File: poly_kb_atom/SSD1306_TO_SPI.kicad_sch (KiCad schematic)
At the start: 11 parts, among them J1 Conn_01x16, SW1 SW_Push

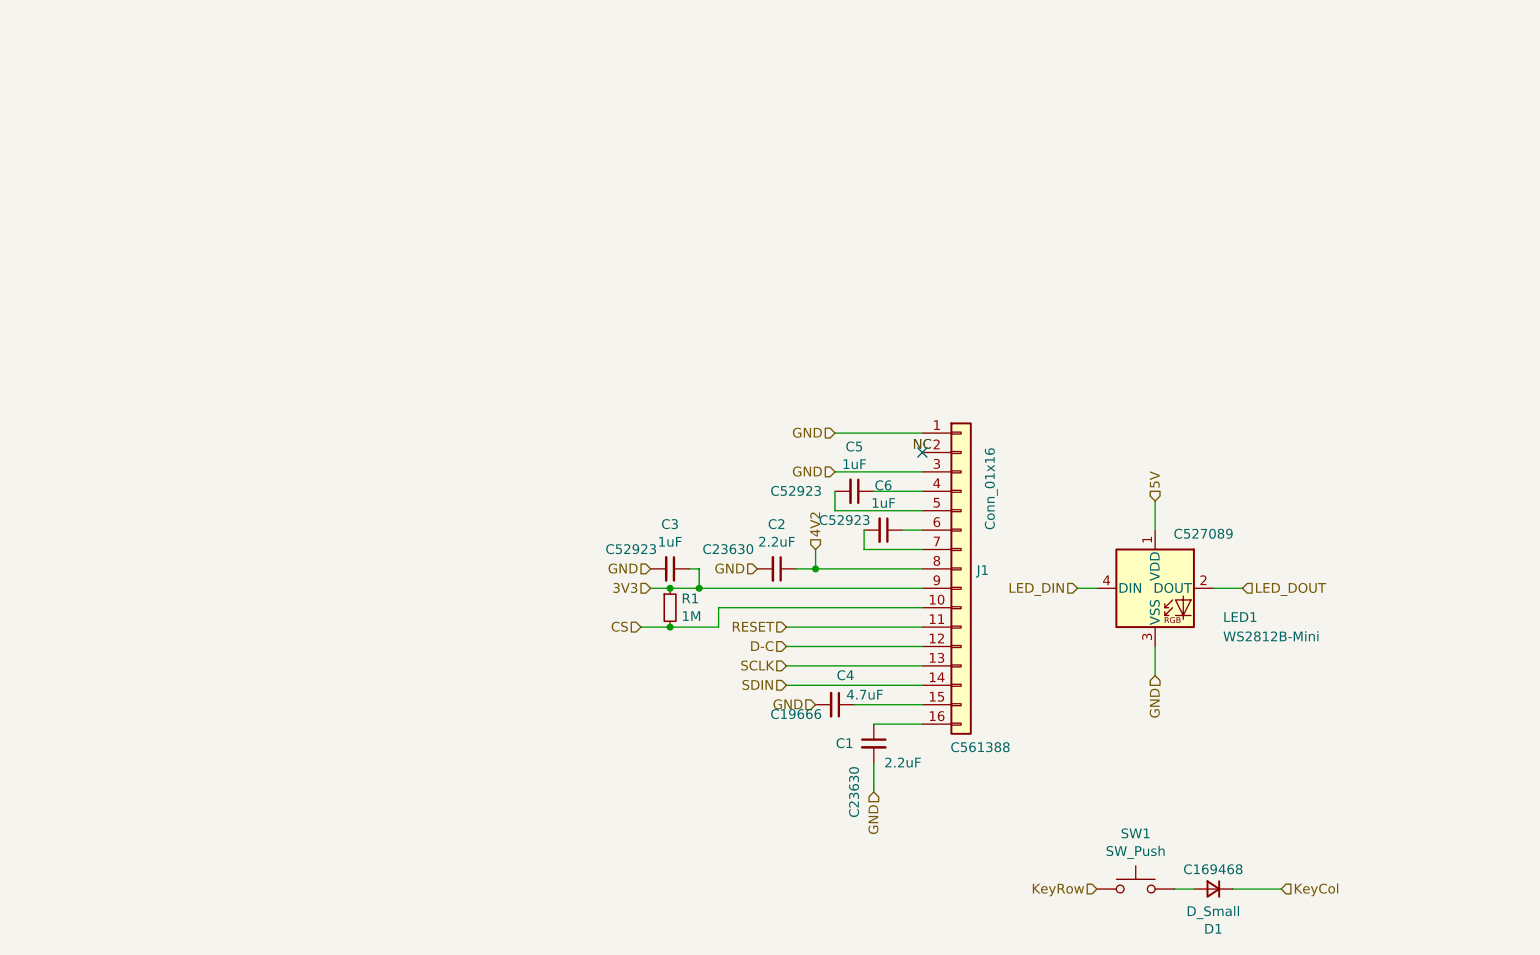
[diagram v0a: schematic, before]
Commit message: Added new revisions for all pcbs expect 1.25U; cleaned up gerber dirs
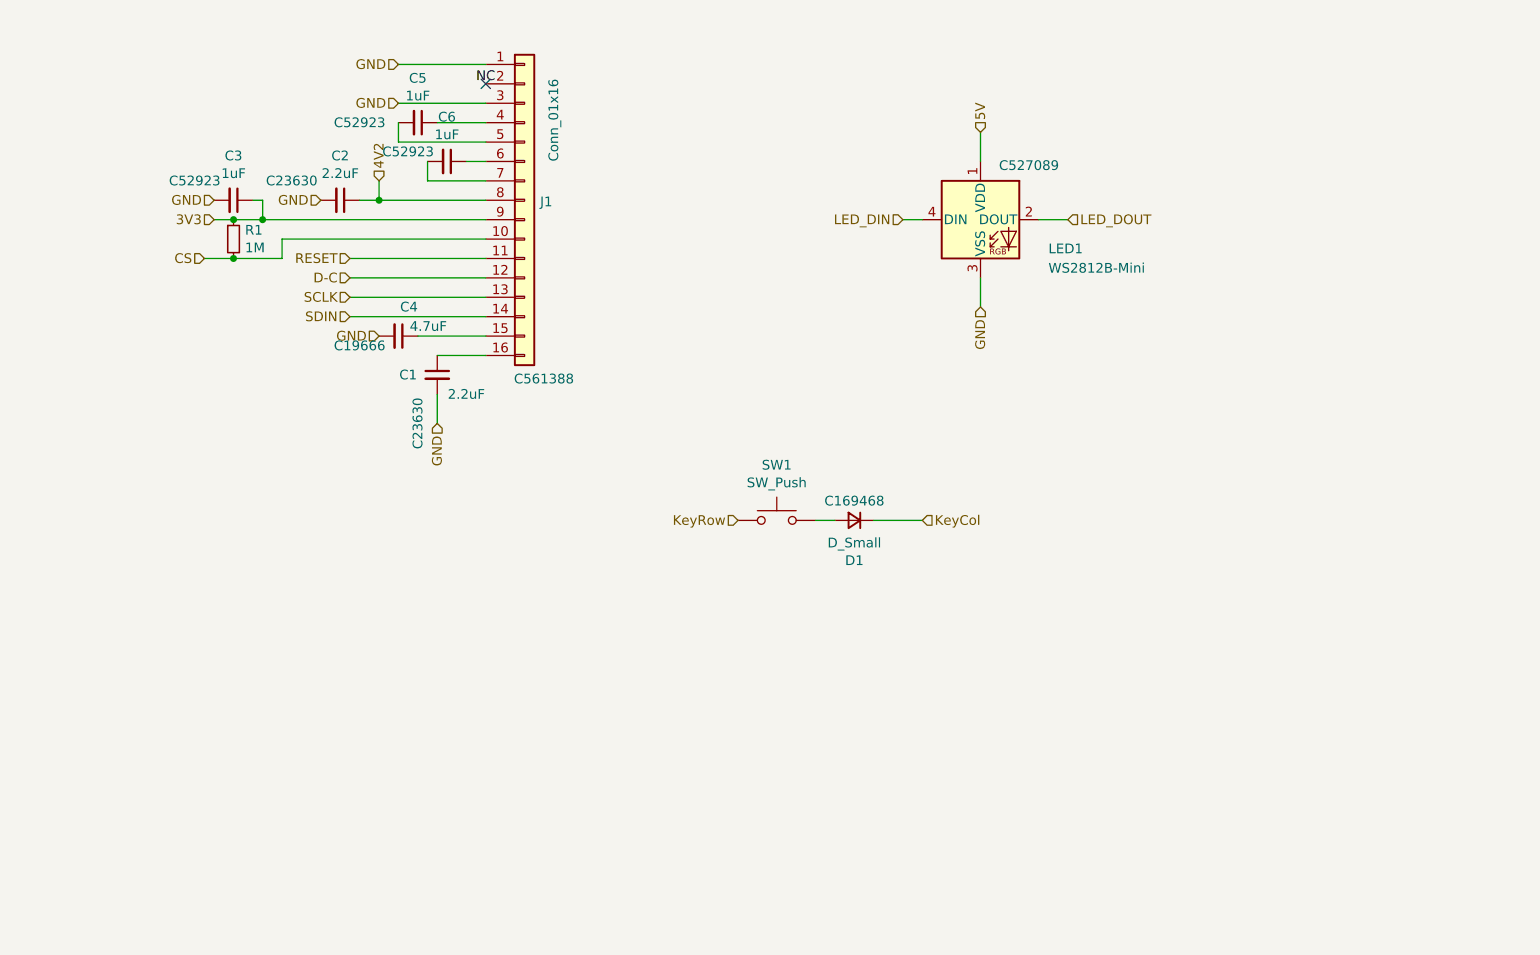
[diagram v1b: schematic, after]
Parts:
- D1: footprint Diode_SMD:D_SOD-323 -> poly_kb:D_SOD-323Ext
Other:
- moved on the sheet: C1, C2, C3, C4, C5, C6, D1, J1, LED1, R1, SW1

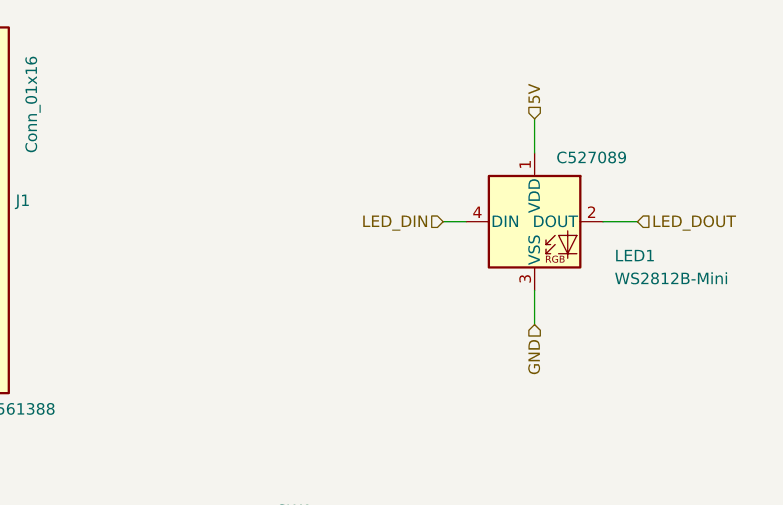
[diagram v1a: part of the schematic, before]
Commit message: Added optional C7 and fix LED silkscreens
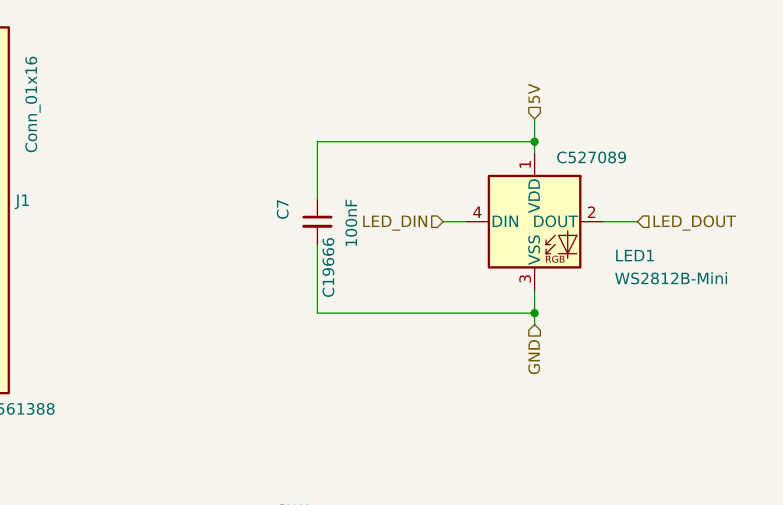
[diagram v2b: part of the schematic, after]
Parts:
- added C7: 100nF, Capacitor_SMD:C_0603_1608Metric, symbol Device:C_Small
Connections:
- net 5V: now also C7.1
- net GND: now also C7.2
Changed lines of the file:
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@@
     (company "thpoll")
   )
+  (junction (at 139.7 40.64) (diameter 0) (color 0 0 0 0)
+  )
   (junction (at 60.96 46.99) (diameter 0) (color 0 0 0 0)
   )
@@
   (junction (at 45.72 49.53) (diameter 0) (color 0 0 0 0)
   )
+  (junction (at 139.7 59.69) (diameter 0) (color 0 0 0 0)
+  )
   (no_connect (at 74.93 31.75))
+  (wire (pts (xy 139.7 40.64) (xy 139.7 41.91))
+    (stroke (width 0) (type default) (color 0 0 0 0))
+  )
   (wire (pts (xy 74.93 54.61) (xy 57.15 54.61))
     (stroke (width 0) (type default) (color 0 0 0 0))
   )
+  (wire (pts (xy 139.7 59.69) (xy 139.7 60.96))
+    (stroke (width 0) (type default) (color 0 0 0 0))
+  )
   (wire (pts (xy 45.72 46.99) (xy 44.45 46.99))
     (stroke (width 0) (type default) (color 0 0 0 0))
@@
     (stroke (width 0) (type default) (color 0 0 0 0))
   )
-  (wire (pts (xy 139.7 38.1) (xy 139.7 41.91))
+  (wire (pts (xy 139.7 38.1) (xy 139.7 40.64))
     (stroke (width 0) (type default) (color 0 0 0 0))
   )
@@
     (stroke (width 0) (type default) (color 0 0 0 0))
   )
+  (wire (pts (xy 115.57 40.64) (xy 115.57 46.99))
+    (stroke (width 0) (type default) (color 0 0 0 0))
+  )
+  (wire (pts (xy 115.57 59.69) (xy 139.7 59.69))
+    (stroke (width 0) (type default) (color 0 0 0 0))
+  )
   (wire (pts (xy 74.93 57.15) (xy 57.15 57.15))
     (stroke (width 0) (type default) (color 0 0 0 0))
@@
     (stroke (width 0) (type default) (color 0 0 0 0))
   )
+  (wire (pts (xy 115.57 52.07) (xy 115.57 59.69))
+    (stroke (width 0) (type default) (color 0 0 0 0))
+  )
   (wire (pts (xy 74.93 41.91) (xy 72.39 41.91))
     (stroke (width 0) (type default) (color 0 0 0 0))
@@
     (stroke (width 0) (type default) (color 0 0 0 0))
   )
-  (wire (pts (xy 139.7 57.15) (xy 139.7 60.96))
+  (wire (pts (xy 139.7 57.15) (xy 139.7 59.69))
     (stroke (width 0) (type default) (color 0 0 0 0))
   )
@@
   )
   (wire (pts (xy 45.72 46.99) (xy 45.72 49.53))
+    (stroke (width 0) (type default) (color 0 0 0 0))
+  )
+  (wire (pts (xy 139.7 40.64) (xy 115.57 40.64))
     (stroke (width 0) (type default) (color 0 0 0 0))
   )
@@
     (pin "1")
     (pin "2")
+  )
+  (symbol (lib_id "Device:C_Small") (at 115.57 49.53 0) (unit 1)
+    (in_bom yes) (on_board yes)
+    (property "Reference" "C7" (id 0) (at 111.76 46.99 90)
+      (effects (font (size 1.27 1.27)) (justify right))
+    )
+    (property "Value" "100nF" (id 1) (at 119.38 46.99 90)
+      (effects (font (size 1.27 1.27)) (justify right))
+    )
+    (property "Footprint" "Capacitor_SMD:C_0603_1608Metric" (id 2) (at 115.57 49.53 0)
+      (effects (font (size 1.27 1.27)) hide)
+    )
+    (property "Datasheet" "~" (id 3) (at 115.57 49.53 0)
+      (effects (font (size 1.27 1.27)) hide)
+    )
+    (property "LCSC" "C19666" (id 4) (at 116.84 54.61 90))
+    (pin "1")
+    (pin "2")

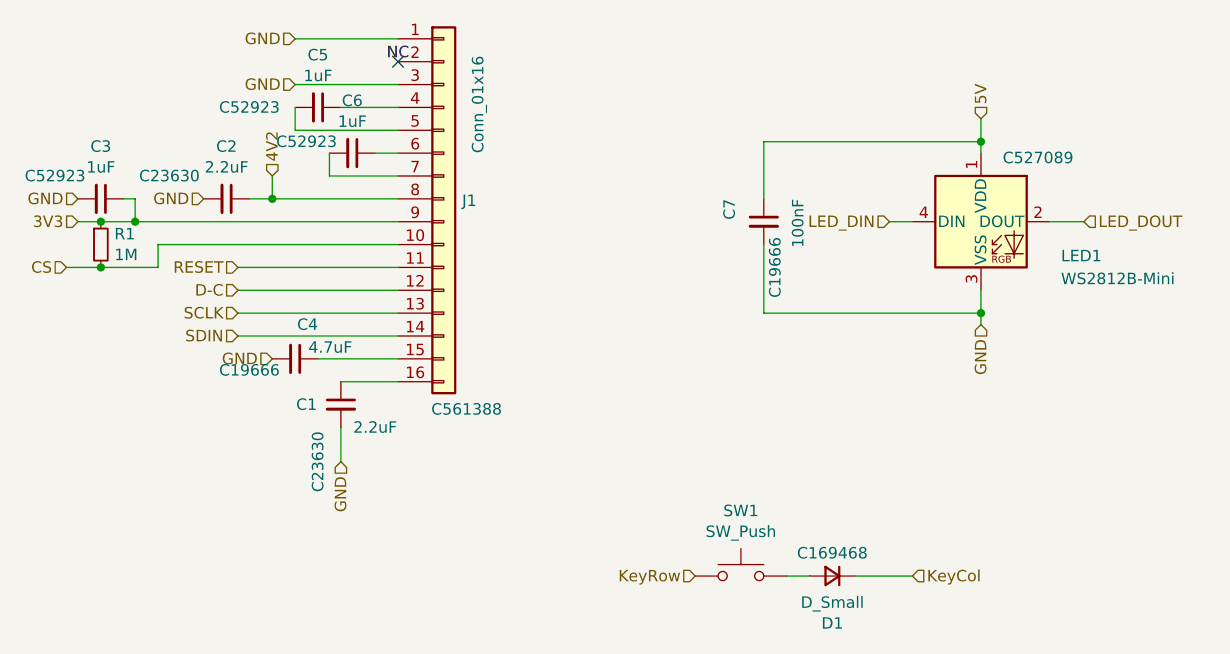
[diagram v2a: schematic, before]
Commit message: Reorganized 3rd party, added poly_kb_wave project;
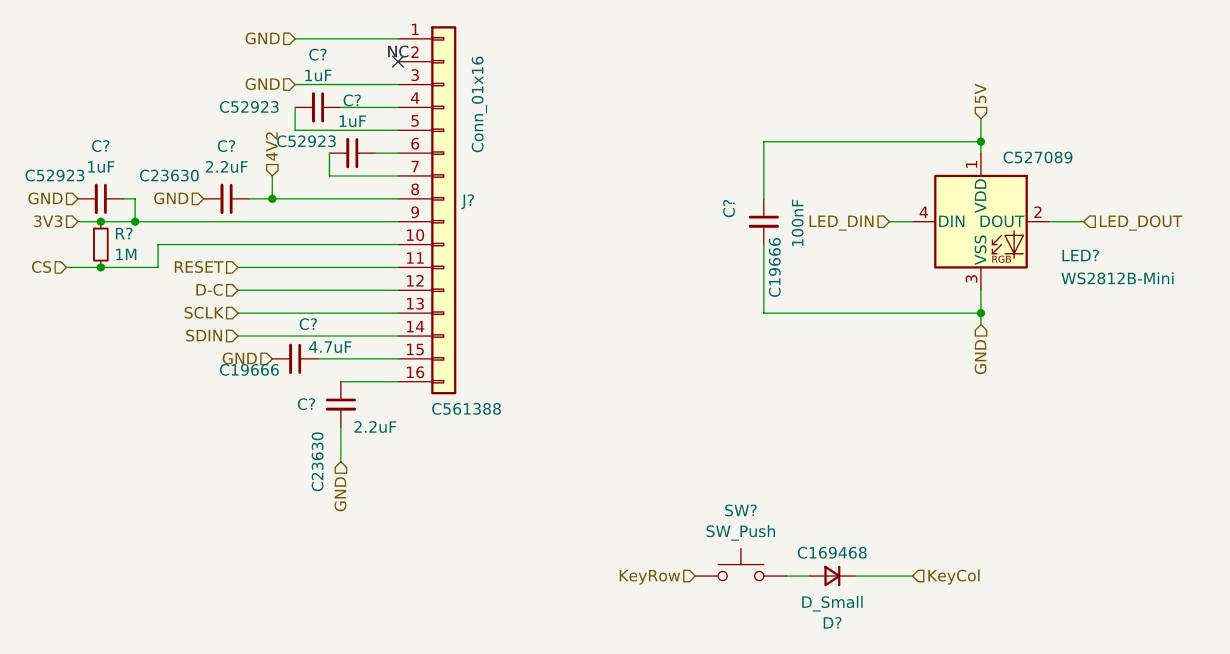
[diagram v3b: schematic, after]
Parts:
- renumbered C6 to C?, C4 to C?, C1 to C?, C5 to C?, C2 to C?, C3 to C?, C7 to C?, D1 to D?, J1 to J?, LED1 to LED?, R1 to R?, SW1 to SW?
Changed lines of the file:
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@@
     (effects (font (size 1.27 1.27)) (justify right))
   )
-  (symbol (lib_id "Connector_Generic:Conn_01x16") (at 80.01 46.99 0) (unit 1)
+  (symbol (lib_id "Connector_Generic:Conn_01x16") (at 80.01 46.99 0)
     (in_bom yes) (on_board yes)
-    (property "Reference" "J1" (id 0) (at 82.042 47.1932 0)
+    (property "Reference" "J?" (id 0) (at 82.042 47.1932 0)
       (effects (font (size 1.27 1.27)) (justify left))
     )
@@
     (pin "9")
   )
-  (symbol (lib_id "Device:C_Small") (at 69.85 41.91 270) (unit 1)
+  (symbol (lib_id "Device:C_Small") (at 69.85 41.91 270)
     (in_bom yes) (on_board yes)
-    (property "Reference" "C6" (id 0) (at 69.85 36.0934 90))
+    (property "Reference" "C?" (id 0) (at 69.85 36.0934 90))
     (property "Value" "1uF" (id 1) (at 69.85 38.4048 90))
     (property "Footprint" "Capacitor_SMD:C_0402_1005Metric" (id 2) (at 69.85 41.91 0)
@@
     (pin "2")
   )
-  (symbol (lib_id "LED:WS2812B") (at 139.7 49.53 0) (unit 1)
+  (symbol (lib_id "LED:WS2812B") (at 139.7 49.53 0)
     (in_bom yes) (on_board yes)
-    (property "Reference" "LED1" (id 0) (at 148.59 53.34 0)
+    (property "Reference" "LED?" (id 0) (at 148.59 53.34 0)
       (effects (font (size 1.27 1.27)) (justify left))
     )
@@
     (pin "4")
   )
-  (symbol (lib_id "Device:C_Small") (at 63.5 64.77 270) (unit 1)
+  (symbol (lib_id "Device:C_Small") (at 63.5 64.77 270)
     (in_bom yes) (on_board yes)
-    (property "Reference" "C4" (id 0) (at 66.04 60.96 90)
+    (property "Reference" "C?" (id 0) (at 66.04 60.96 90)
       (effects (font (size 1.27 1.27)) (justify right))
     )
@@
     (pin "2")
   )
-  (symbol (lib_id "Device:C_Small") (at 68.58 69.85 0) (unit 1)
+  (symbol (lib_id "Device:C_Small") (at 68.58 69.85 0)
     (in_bom yes) (on_board yes)
-    (property "Reference" "C1" (id 0) (at 64.77 69.85 0))
+    (property "Reference" "C?" (id 0) (at 64.77 69.85 0))
     (property "Value" "2.2uF" (id 1) (at 72.39 72.39 0))
     (property "Footprint" "Capacitor_SMD:C_0603_1608Metric" (id 2) (at 68.58 69.85 0)
@@
     (pin "2")
   )
-  (symbol (lib_id "Device:C_Small") (at 66.04 36.83 270) (unit 1)
+  (symbol (lib_id "Device:C_Small") (at 66.04 36.83 270)
     (in_bom yes) (on_board yes)
-    (property "Reference" "C5" (id 0) (at 66.04 31.0134 90))
+    (property "Reference" "C?" (id 0) (at 66.04 31.0134 90))
     (property "Value" "1uF" (id 1) (at 66.04 33.3248 90))
     (property "Footprint" "Capacitor_SMD:C_0402_1005Metric" (id 2) (at 66.04 36.83 0)
@@
     (pin "2")
   )
-  (symbol (lib_id "Device:C_Small") (at 55.88 46.99 270) (unit 1)
+  (symbol (lib_id "Device:C_Small") (at 55.88 46.99 270)
     (in_bom yes) (on_board yes)
-    (property "Reference" "C2" (id 0) (at 55.88 41.1734 90))
+    (property "Reference" "C?" (id 0) (at 55.88 41.1734 90))
     (property "Value" "2.2uF" (id 1) (at 55.88 43.4848 90))
     (property "Footprint" "Capacitor_SMD:C_0603_1608Metric" (id 2) (at 55.88 46.99 0)
@@
     (pin "2")
   )
-  (symbol (lib_id "Device:C_Small") (at 41.91 46.99 270) (unit 1)
+  (symbol (lib_id "Device:C_Small") (at 41.91 46.99 270)
     (in_bom yes) (on_board yes)
-    (property "Reference" "C3" (id 0) (at 41.91 41.1734 90))
+    (property "Reference" "C?" (id 0) (at 41.91 41.1734 90))
     (property "Value" "1uF" (id 1) (at 41.91 43.4848 90))
     (property "Footprint" "Capacitor_SMD:C_0402_1005Metric" (id 2) (at 41.91 46.99 0)
@@
     (pin "2")
   )
-  (symbol (lib_id "Switch:SW_Push") (at 113.03 88.9 0) (unit 1)
+  (symbol (lib_id "Switch:SW_Push") (at 113.03 88.9 0)
     (in_bom yes) (on_board yes)
-    (property "Reference" "SW1" (id 0) (at 113.03 81.661 0))
+    (property "Reference" "SW?" (id 0) (at 113.03 81.661 0))
     (property "Value" "SW_Push" (id 1) (at 113.03 83.9724 0))
     (property "Footprint" "poly_kb:SW_Cherry_MX_1.00u_PCB_NoSilk" (id 2) (at 113.03 83.82 0)
@@
     (pin "2")
   )
-  (symbol (lib_id "Device:D_Small") (at 123.19 88.9 180) (unit 1)
+  (symbol (lib_id "Device:D_Small") (at 123.19 88.9 180)
     (in_bom yes) (on_board yes)
-    (property "Reference" "D1" (id 0) (at 123.19 94.1578 0))
+    (property "Reference" "D?" (id 0) (at 123.19 94.1578 0))
     (property "Value" "D_Small" (id 1) (at 123.19 91.8464 0))
     (property "Footprint" "poly_kb:D_SOD-323Ext" (id 2) (at 123.19 88.9 90)
@@
     (pin "2")
   )
-  (symbol (lib_id "Device:C_Small") (at 115.57 49.53 0) (unit 1)
+  (symbol (lib_id "Device:C_Small") (at 115.57 49.53 0)
     (in_bom yes) (on_board yes)
-    (property "Reference" "C7" (id 0) (at 111.76 46.99 90)
+    (property "Reference" "C?" (id 0) (at 111.76 46.99 90)
       (effects (font (size 1.27 1.27)) (justify right))
     )
@@
     (pin "2")
   )
-  (symbol (lib_id "Device:R_Small") (at 41.91 52.07 0) (unit 1)
+  (symbol (lib_id "Device:R_Small") (at 41.91 52.07 0)
     (in_bom yes) (on_board yes)
-    (property "Reference" "R1" (id 0) (at 43.4086 50.9016 0)
+    (property "Reference" "R?" (id 0) (at 43.4086 50.9016 0)
       (effects (font (size 1.27 1.27)) (justify left))
     )

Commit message: split kb prototype, left side
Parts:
- C7_1: renamed from C?; value 100nF -> DNP
- CONN1: renamed from J?; value Conn_01x16 -> 0.42" Display Connector
- R1_1: renamed from R?; value 1M -> 10k
- SW_K_1: renamed from SW?; value SW_Push -> CheeryMX KeySwitch
- gave numbers to parts that had none: 8
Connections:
- net VCOMH: now reaches C4_1.1, CONN1.15 (Pin_15)
- net VCC: now reaches C1_1.1, CONN1.16 (Pin_16)
- net C2P: now reaches C5_1.1, CONN1.4 (Pin_4)
- net C2N: now reaches C5_1.2, CONN1.5 (Pin_5)
- net C1P: now reaches C6_1.1, CONN1.6 (Pin_6)
- net C1N: now reaches C6_1.2, CONN1.7 (Pin_7)
- net SW-D: now reaches D1_1.2 (A), SW_K_1.2
- net 3V3 renamed VDD
- net 4V2 renamed VBAT
- net 5V renamed VLED
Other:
- note added: "Opt. 100nF"
- moved on the sheet: C1_1, C2_1, C3_1, C4_1, C5_1, C6_1, C7_1, CONN1, D1_1, LED1, R1_1, SW_K_1
